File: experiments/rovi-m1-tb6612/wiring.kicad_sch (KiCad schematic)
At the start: 4 parts, among them M1 DC_MOTOR, U1 ESP32S3, U2 TB6612FNG

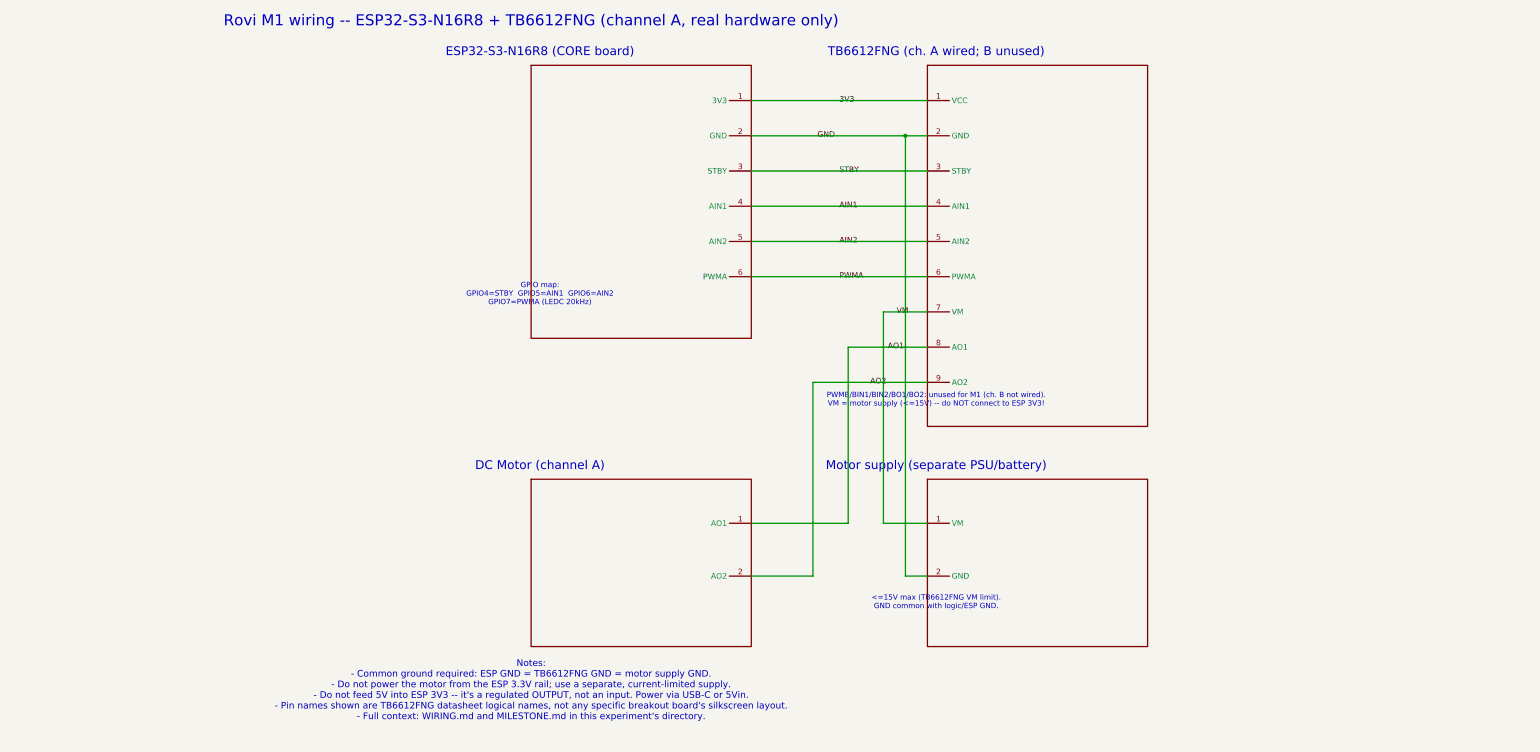
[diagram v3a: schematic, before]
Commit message: wiring.kicad_sch: model the complete physical pinout of both boards
The previous version's symbols only had the ~6-9 pins M1 actually
uses, arbitrarily numbered (Pin 1, Pin 2, ...) -- not the boards the
user actually purchased. Holding the physical board next to that
diagram, the pin count and numbering didn't match, so "pin 3" in the
schematic meant nothing on the silkscreen.

Rebuilt both symbols as complete, accurate representations of
docs/reference/: ESP32-S3-N16R8 now has all 44 pins (22 per header,
same top-to-bottom order as the real board), TB6612FNG has all 16 (8
per header). Pin names are the literal silkscreened labels (e.g. "4",
"3V3", "5Vin", "PWMA", "VCC"); pin numbers (L1..L22/R1..R22,
L1..L8/R1..R8) are physical header positions for cross-referencing,
not chip pin numbers. All 45 pins M1 doesn't use get explicit
no-connect flags rather than being silently omitted.

Since the real boards' pin orders don't align row-for-row (TB6612FNG's
left header runs PWMA/AIN2/AIN1/STBY while ESP32-S3's relevant rows
run STBY/AIN1/AIN2/PWMA -- reversed), most of the 9 routed nets needed
real bends instead of straight lines; 3V3 routes around TB6612FNG's
top edge since VCC sits on the *opposite* header from the signal pins.
Paper bumped to A3 to fit two full-pinout boards plus the routing.

Hit two rounds of the same self-inflicted bug: a net label placed
exactly on top of a different net's wire silently merges the two
nets (KiCad attaches a label to whatever wire is under it). First
occurrence merged VM into GND (caught last session). Second
occurrence, mid-rebuild here, merged STBY into AIN2 -- caught this
time via `kicad-cli sch export netlist` (the authoritative connectivity
source) before it ever reached a commit.

Generated the file with a scratch Python script (not committed --
one-off, not a maintained build tool) rather than hand-writing ~60
pins across two symbols plus 45 no-connect markers.

Verified: kicad-cli sch erc 0 errors/0 connectivity warnings; sc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
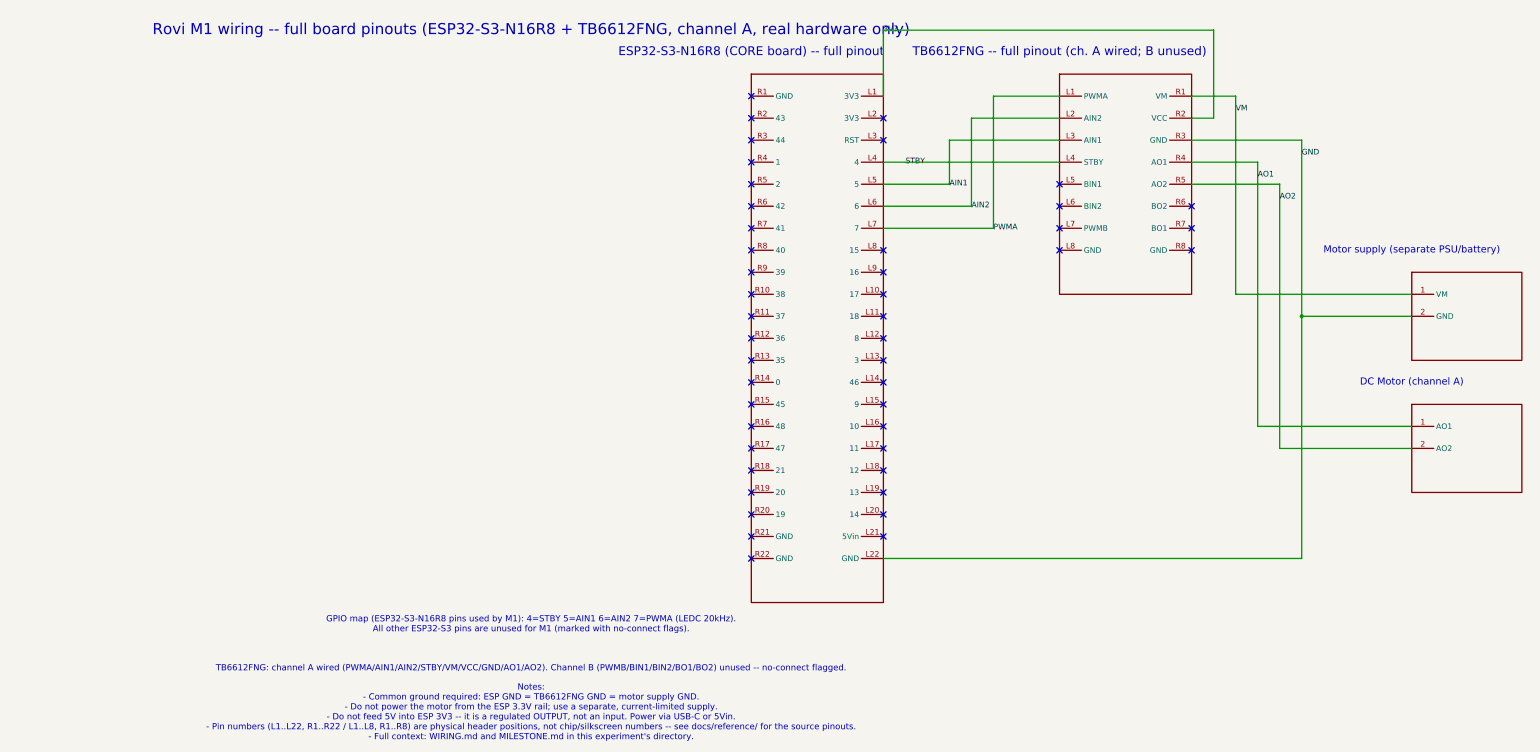
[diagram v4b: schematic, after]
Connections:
- net 3V3: now also U1.L1 (3V3), U2.R2 (VCC); no longer U1.1 (3V3), U2.1 (VCC)
- net AIN1: now also U1.L5 (5), U2.L3 (AIN1); no longer U1.4 (AIN1), U2.4 (AIN1)
- net AIN2: now also U1.L6 (6), U2.L2 (AIN2); no longer U1.5 (AIN2), U2.5 (AIN2)
- net AO1: now also U2.R4 (AO1); no longer U2.8 (AO1)
- net AO2: now also U2.R5 (AO2); no longer U2.9 (AO2)
- net GND: now also U1.L22 (GND), U2.R3 (GND); no longer U1.2 (GND), U2.2 (GND)
- net PWMA: now also U1.L7 (7), U2.L1 (PWMA); no longer U1.6 (PWMA), U2.6 (PWMA)
- net STBY: now also U1.L4 (4), U2.L4 (STBY); no longer U1.3 (STBY), U2.3 (STBY)
- net VM: now also U2.R1 (VM); no longer U2.7 (VM)
- no-connect marks 0 -> 45
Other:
- note added: "ESP32-S3-N16R8 (CORE board) -- full pinout"
- note added: "GPIO map (ESP32-S3-N16R8 pins used by M1): 4=STBY 5=AIN1 6=AIN2 7=PWMA (LEDC 20kHz). All other ESP32-S3 pins are unused for M1 (marked with no-connect flags)."
- note added: "Notes: - Common ground required: ESP GND = TB6612FNG GND = motor supply GND. - Do not power the motor from the ESP 3.3V rail; use a separate, current-limited supply. - Do not feed 5V into ESP 3V3 -- it is a regulated OUTPUT, not an input. Power via USB-C or 5Vin. - Pin numbers (L1..L22, R1..R22 / L1..L8, R1..R8) are physical header positions, not chip/silkscreen numbers -- see docs/reference/ for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"
- note added: "Rovi M1 wiring -- full board pinouts (ESP32-S3-N16R8 + TB6612FNG, channel A, real hardware only)"
- note added: "TB6612FNG -- full pinout (ch. A wired; B unused)"
- note added: "TB6612FNG: channel A wired (PWMA/AIN1/AIN2/STBY/VM/VCC/GND/AO1/AO2). Channel B (PWMB/BIN1/BIN2/BO1/BO2) unused -- no-connect flagged."
- note removed: "<=15V max (TB6612FNG VM limit). GND common with logic/ESP GND."
- note removed: "ESP32-S3-N16R8 (CORE board)"
- note removed: "GPIO map: GPIO4=STBY GPIO5=AIN1 GPIO6=AIN2 GPIO7=PWMA (LEDC 20kHz)"
- note removed: "Notes: - Common ground required: ESP GND = TB6612FNG GND = motor supply GND. - Do not power the motor from the ESP 3.3V rail; use a separate, current-limited supply. - Do not feed 5V into ESP 3V3 -- it's a regulated OUTPUT, not an input. Power via USB-C or 5Vin. - Pin names shown are TB6612FNG datasheet logical names, not any specific breakout board's silkscreen layout. - Full context: WIRING.md 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"
- note removed: "PWMB/BIN1/BIN2/BO1/BO2: unused for M1 (ch. B not wired). VM = motor supply (<=15V) -- do NOT connect to ESP 3V3!"
- note removed: "Rovi M1 wiring -- ESP32-S3-N16R8 + TB6612FNG (channel A, real hardware only)"
- note removed: "TB6612FNG (ch. A wired; B unused)"
